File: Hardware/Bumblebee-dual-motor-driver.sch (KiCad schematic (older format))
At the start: 49 parts, among them J1 ICSP, J10 GND, J11 MOTOR1_A, J12 MOTOR1_B, J13 MOTOR2_A, J14 MOTOR2_B, J15 MAIN+, J16 MAIN-, J2 USB_B_Micro, J3 HEADER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

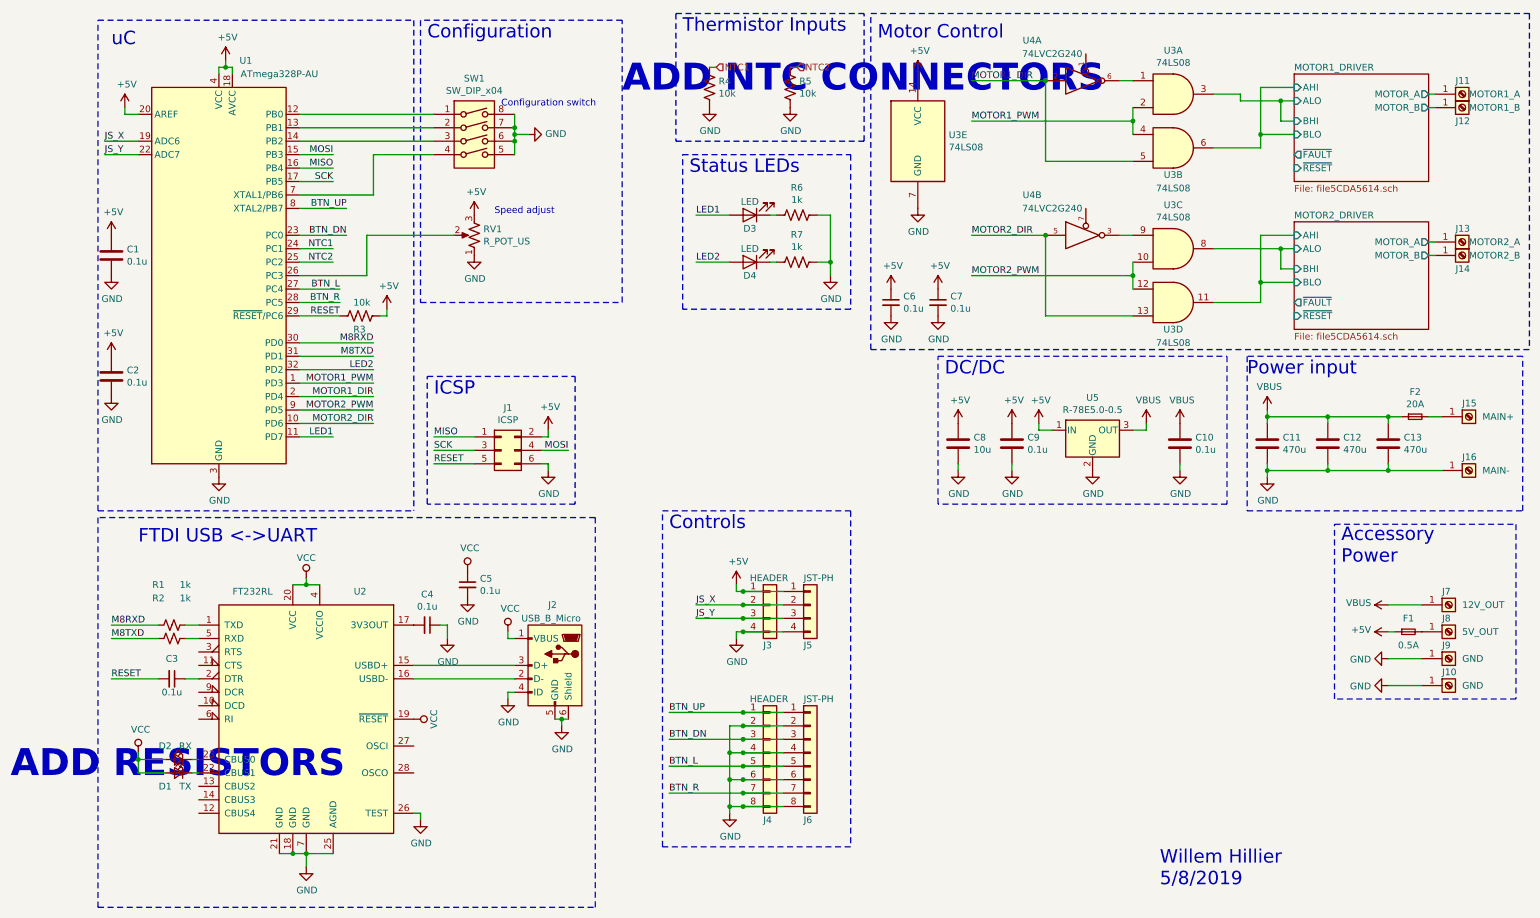
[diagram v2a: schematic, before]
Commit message: Fixed small issues and started laying out H-bridge
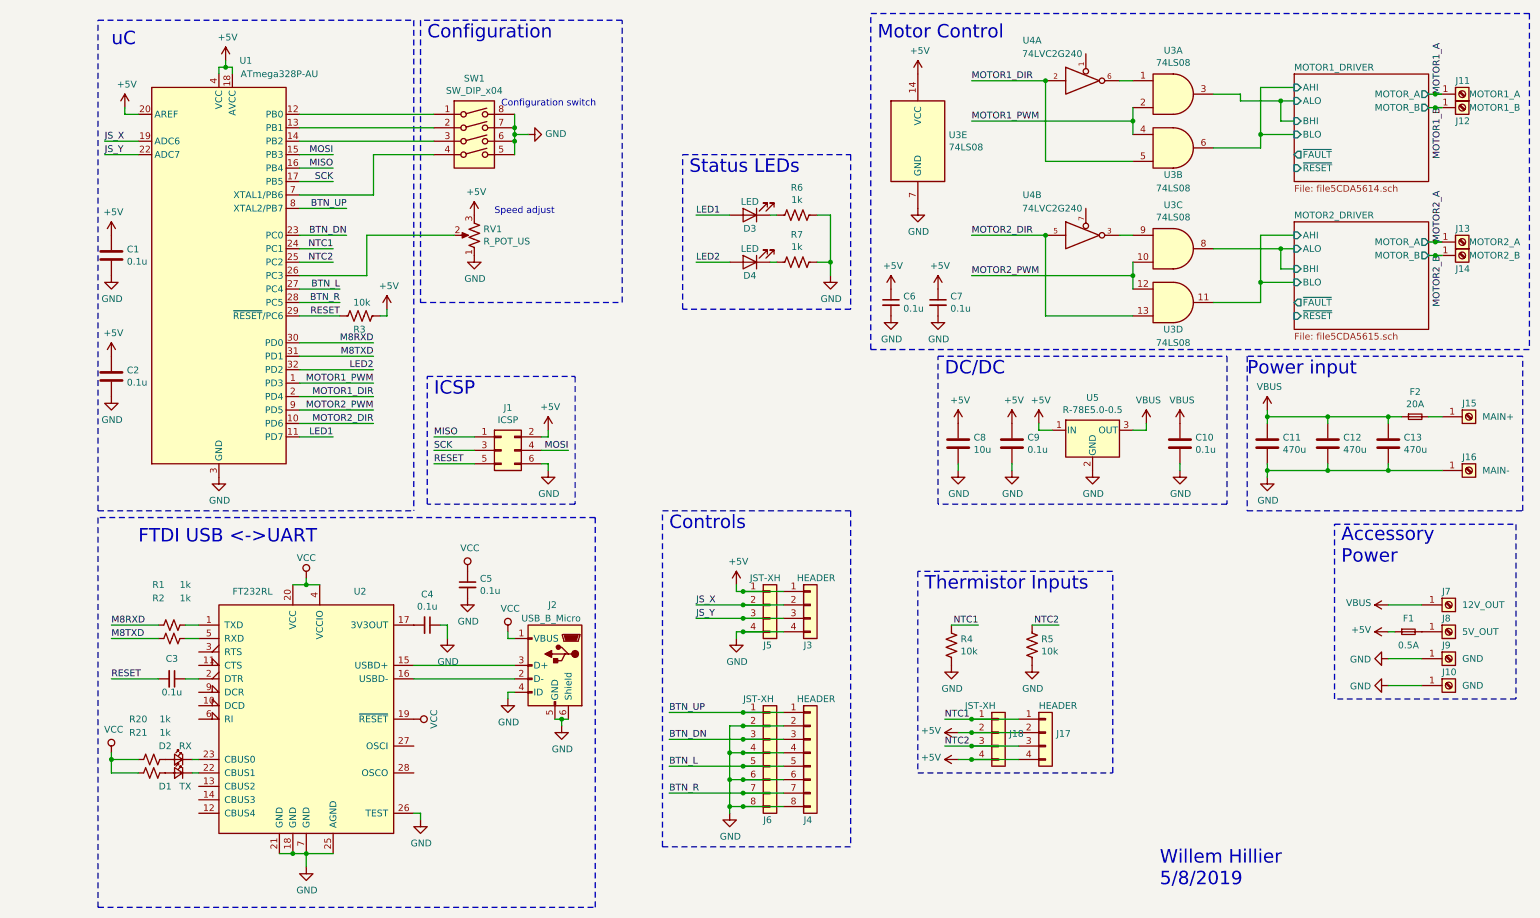
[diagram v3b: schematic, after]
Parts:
- added J17: HEADER, TerminalBlock_TE-Connectivity:TerminalBlock_TE_282834-4_1x04_P2.54mm_Horizontal, symbol Connector_Generic:Conn_01x04
- added J18: JST-XH, Connector_JST:JST_XH_B4B-XH-A_1x04_P2.50mm_Vertical, symbol Connector_Generic:Conn_01x04
- added R20, R21: 1k, Resistor_SMD:R_0603_1608Metric, symbol Device:R_Small_US
- J3: footprint Connector_PinSocket_2.54mm:PinSocket_1x04_P2.54mm_Vertical -> TerminalBlock_TE-Connectivity:TerminalBlock_TE_282834-4_1x04_P2.54mm_Horizontal
- J4: footprint Connector_PinSocket_2.54mm:PinSocket_1x08_P2.54mm_Vertical -> TerminalBlock_TE-Connectivity:TerminalBlock_TE_282834-8_1x08_P2.54mm_Horizontal
- J5, J6: value JST-PH -> JST-XH
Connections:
- net +5V: now also J17.2 (Pin_2), J17.4 (Pin_4), J18.2 (Pin_2), J18.4 (Pin_4)
- net NTC1: now also J17.1 (Pin_1), J18.1 (Pin_1)
- net NTC2: now also J17.3 (Pin_3), J18.3 (Pin_3)
- net VCC: now also R20.2, R21.2; no longer D1.2 (A), D2.2 (A)
- net MOTOR1_DRIVER/MOTOR_A renamed MOTOR1_A
- net MOTOR1_DRIVER/MOTOR_B renamed MOTOR1_B
- net MOTOR2_DRIVER/MOTOR_A renamed MOTOR2_A
- net MOTOR2_DRIVER/MOTOR_B renamed MOTOR2_B
- new net: D1.2 (A), R20.1
- new net: D2.2 (A), R21.1
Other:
- note removed: "ADD NTC CONNECTORS"
- note removed: "ADD RESISTORS"
- moved on the sheet: J3, J4, J5, J6, R4, R5
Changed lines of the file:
@@
 L Device:R_US R?
 U 1 1 5C53D9DB
-P 5100 1050
+P 6900 5200
 AR Path="/5C4E5628/5C53D9DB" Ref="R?"  Part="1"
 AR Path="/5C83278E/5C8304A7/5C53D9DB" Ref="R?"  Part="1"
 AR Path="/5C53D9DB" Ref="R4"  Part="1"
-F 0 "R4" H 5032 1004 50  0000 R CNN
-F 1 "10k" H 5032 1095 50  0000 R CNN
-F 2 "Resistor_SMD:R_0603_1608Metric" V 5140 1040 50  0001 C CNN
-F 3 "~" H 5100 1050 50  0001 C CNN
-	1    5100 1050
+F 0 "R4" H 6832 5154 50  0000 R CNN
+F 1 "10k" H 6832 5245 50  0000 R CNN
+F 2 "Resistor_SMD:R_0603_1608Metric" V 6940 5190 50  0001 C CNN
+F 3 "~" H 6900 5200 50  0001 C CNN
+	1    6900 5200
 	-1   0    0    1
 $EndComp
@@
 L power:GND #PWR?
 U 1 1 5C540E62
-P 5100 1200
+P 6900 5350
 AR Path="/5C4E5628/5C540E62" Ref="#PWR?"  Part="1"
 AR Path="/5C83278E/5C8304A7/5C540E62" Ref="#PWR?"  Part="1"
 AR Path="/5C540E62" Ref="#PWR025"  Part="1"
-F 0 "#PWR025" H 5100 950 50  0001 C CNN
-F 1 "GND" H 5105 1027 50  0000 C CNN
-F 2 "" H 5100 1200 50  0001 C CNN
-F 3 "" H 5100 1200 50  0001 C CNN
-	1    5100 1200
+F 0 "#PWR025" H 6900 5100 50  0001 C CNN
+F 1 "GND" H 6905 5177 50  0000 C CNN
+F 2 "" H 6900 5350 50  0001 C CNN
+F 3 "" H 6900 5350 50  0001 C CNN
+	1    6900 5350
 	1    0    0    -1
 $EndComp
@@
 L Device:R_US R?
 U 1 1 5C5485A4
-P 5700 1050
+P 7500 5200
 AR Path="/5C4E5628/5C5485A4" Ref="R?"  Part="1"
 AR Path="/5C83278E/5C8304A7/5C5485A4" Ref="R?"  Part="1"
 AR Path="/5C5485A4" Ref="R5"  Part="1"
-F 0 "R5" H 5632 1004 50  0000 R CNN
-F 1 "10k" H 5632 1095 50  0000 R CNN
-F 2 "Resistor_SMD:R_0603_1608Metric" V 5740 1040 50  0001 C CNN
-F 3 "~" H 5700 1050 50  0001 C CNN
-	1    5700 1050
+F 0 "R5" H 7432 5154 50  0000 R CNN
+F 1 "10k" H 7432 5245 50  0000 R CNN
+F 2 "Resistor_SMD:R_0603_1608Metric" V 7540 5190 50  0001 C CNN
+F 3 "~" H 7500 5200 50  0001 C CNN
+	1    7500 5200
 	-1   0    0    1
 $EndComp
@@
 L power:GND #PWR?
 U 1 1 5C5485BA
-P 5700 1200
+P 7500 5350
 AR Path="/5C4E5628/5C5485BA" Ref="#PWR?"  Part="1"
 AR Path="/5C83278E/5C8304A7/5C5485BA" Ref="#PWR?"  Part="1"
 AR Path="/5C5485BA" Ref="#PWR029"  Part="1"
-F 0 "#PWR029" H 5700 950 50  0001 C CNN
-F 1 "GND" H 5705 1027 50  0000 C CNN
-F 2 "" H 5700 1200 50  0001 C CNN
-F 3 "" H 5700 1200 50  0001 C CNN
-	1    5700 1200
+F 0 "#PWR029" H 7500 5100 50  0001 C CNN
+F 1 "GND" H 7505 5177 50  0000 C CNN
+F 2 "" H 7500 5350 50  0001 C CNN
+F 3 "" H 7500 5350 50  0001 C CNN
+	1    7500 5350
 	1    0    0    -1
 $EndComp
@@
 Wire Notes Line
 	550  4200 2900 4200
-Text Notes 4900 650  0    100  ~ 0
+Text Notes 6700 4800 0    100  ~ 0
 Thermistor Inputs
-Text HLabel 5150 900  2    50   Input ~ 0
-NTC1
-Wire Wire Line
-	5150 900  5100 900
-Text HLabel 5750 900  2    50   Input ~ 0
-NTC2
-Wire Wire Line
-	5750 900  5700 900
-Wire Notes Line
-	4850 500  6250 500
-Wire Notes Line
-	4850 500  4850 1450
-Wire Notes Line
-	4850 1450 6250 1450
-Wire Notes Line
-	6250 1450 6250 500
 Text Notes 8450 7000 0    100  ~ 0
 Willem Hillier\n5/8/2019
@@
 L Connector_Generic:Conn_01x04 J5
 U 1 1 5CEF2069
-P 5850 4900
-F 0 "J5" H 5800 4600 50  0000 L CNN
-F 1 "JST-PH" H 5800 5100 50  0000 L CNN
-F 2 "Connector_JST:JST_XH_B4B-XH-A_1x04_P2.50mm_Vertical" H 5850 4900 50  0001 C CNN
-F 3 "~" H 5850 4900 50  0001 C CNN
-	1    5850 4900
+P 5550 4900
+F 0 "J5" H 5500 4600 50  0000 L CNN
+F 1 "JST-XH" H 5400 5100 50  0000 L CNN
+F 2 "Connector_JST:JST_XH_B4B-XH-A_1x04_P2.50mm_Vertical" H 5550 4900 50  0001 C CNN
+F 3 "~" H 5550 4900 50  0001 C CNN
+	1    5550 4900
 	1    0    0    -1
 $EndComp
@@
 L Connector_Generic:Conn_01x04 J3
 U 1 1 5CEFCADE
-P 5550 4900
-F 0 "J3" H 5500 4600 50  0000 L CNN
-F 1 "HEADER" H 5400 5100 50  0000 L CNN
-F 2 "Connector_PinSocket_2.54mm:PinSocket_1x04_P2.54mm_Vertical" H 5550 4900 50  0001 C CNN
-F 3 "~" H 5550 4900 50  0001 C CNN
-	1    5550 4900
+P 5850 4900
+F 0 "J3" H 5800 4600 50  0000 L CNN
+F 1 "HEADER" H 5750 5100 50  0000 L CNN
+F 2 "TerminalBlock_TE-Connectivity:TerminalBlock_TE_282834-4_1x04_P2.54mm_Horizontal" H 5850 4900 50  0001 C CNN
+F 3 "~" H 5850 4900 50  0001 C CNN
+	1    5850 4900
 	1    0    0    -1
 $EndComp
@@
 L power:VCC #PWR06
 U 1 1 5CFB0C44
-P 850 6000
-F 0 "#PWR06" H 850 5850 50  0001 C CNN
-F 1 "VCC" H 867 6173 50  0000 C CNN
-F 2 "" H 850 6000 50  0001 C CNN
-F 3 "" H 850 6000 50  0001 C CNN
-	1    850  6000
-	1    0    0    -1
-$EndComp
-Wire Wire Line
-	850  6000 850  6050
-Wire Wire Line
-	850  6050 1050 6050
-Wire Wire Line
-	1050 6150 850  6150
-Wire Wire Line
-	850  6150 850  6050
-Connection ~ 850  6050
+P 650 6000
+F 0 "#PWR06" H 650 5850 50  0001 C CNN
+F 1 "VCC" H 667 6173 50  0000 C CNN
+F 2 "" H 650 6000 50  0001 C CNN
+F 3 "" H 650 6000 50  0001 C CNN
+	1    650  6000
+	1    0    0    -1
+$EndComp
+Wire Wire Line
+	650  6000 650  6050
+Wire Wire Line
+	650  6050 850  6050
+Wire Wire Line
+	850  6150 650  6150
+Wire Wire Line
+	650  6150 650  6050
+Connection ~ 650  6050
 Text Label 650  5050 0    50   ~ 0
 M8RXD
@@
 L Connector_Generic:Conn_01x08 J4
 U 1 1 5D13B745
-P 5550 6000
-F 0 "J4" H 5500 5500 50  0000 L CNN
-F 1 "HEADER" H 5400 6400 50  0000 L CNN
-F 2 "Connector_PinSocket_2.54mm:PinSocket_1x08_P2.54mm_Vertical" H 5550 6000 50  0001 C CNN
-F 3 "~" H 5550 6000 50  0001 C CNN
-	1    5550 6000
-	1    0    0    -1
-$EndComp
-$Comp
-L Connector_Generic:Conn_01x08 J6
-U 1 1 5D13C2EF
 P 5850 6000
-F 0 "J6" H 5800 5500 50  0000 L CNN
-F 1 "JST-PH" H 5800 6400 50  0000 L CNN
-F 2 "Connector_JST:JST_XH_B8B-XH-A_1x08_P2.50mm_Vertical" H 5850 6000 50  0001 C CNN
+F 0 "J4" H 5800 5500 50  0000 L CNN
+F 1 "HEADER" H 5750 6400 50  0000 L CNN
+F 2 "TerminalBlock_TE-Connectivity:TerminalBlock_TE_282834-8_1x08_P2.54mm_Horizontal" H 5850 6000 50  0001 C CNN
 F 3 "~" H 5850 6000 50  0001 C CNN
 	1    5850 6000
@@
 Wire Wire Line
 	5650 6300 5350 6300
-Wire Wire Line
-	5350 6400 5650 6400
-Connection ~ 5350 6400
 Connection ~ 5350 6200
 Connection ~ 5350 6000
@@
 	5250 5800 5250 6000
 Wire Wire Line
-	5250 6400 5350 6400
-Wire Wire Line
 	5250 5800 5350 5800
 $Comp
@@
 U 5D4DF0EE
 F0 "MOTOR2_DRIVER" 50
-F1 "file5CDA5614.sch" 50
+F1 "file5CDA5615.sch" 50
 F2 "AHI" I L 9450 2150 50
 F3 "ALO" I L 9450 2250 50
@@
 Text Notes 3000 700  0    100  ~ 0
 Configuration
-Text Notes -100 6200 0    200  ~ 40
-ADD RESISTORS
-Text Notes 4450 1100 0    200  ~ 40
-ADD NTC CONNECTORS
+$Comp
+L Device:R_Small_US R20
+U 1 1 5CD595B4
+P 950 6050
+F 0 "R20" V 650 5950 50  0000 C CNN
+F 1 "1k" V 650 6150 50  0000 C CNN
+F 2 "Resistor_SMD:R_0603_1608Metric" H 950 6050 50  0001 C CNN
+F 3 "~" H 950 6050 50  0001 C CNN
+	1    950  6050
+	0    1    1    0
+$EndComp
+$Comp
+L Device:R_Small_US R21
+U 1 1 5CD595BA
+P 950 6150
+F 0 "R21" V 650 6050 50  0000 C CNN
+F 1 "1k" V 650 6250 50  0000 C CNN
+F 2 "Resistor_SMD:R_0603_1608Metric" H 950 6150 50  0001 C CNN
+F 3 "~" H 950 6150 50  0001 C CNN
+	1    950  6150
+	0    1    1    0
+$EndComp
+$Comp
+L Connector_Generic:Conn_01x04 J17
+U 1 1 5CD7FE91
+P 7600 5850
+F 0 "J17" H 7680 5842 50  0000 L CNN
+F 1 "HEADER" H 7550 6050 50  0000 L CNN
+F 2 "TerminalBlock_TE-Connectivity:TerminalBlock_TE_282834-4_1x04_P2.54mm_Horizontal" H 7600 5850 50  0001 C CNN
+F 3 "~" H 7600 5850 50  0001 C CNN
+	1    7600 5850
+	1    0    0    -1
+$EndComp
+Text Label 7100 5050 2    50   ~ 0
+NTC1
+Text Label 7700 5050 2    50   ~ 0
+NTC2
+Wire Wire Line
+	6900 5050 7100 5050
+Wire Wire Line
+	7500 5050 7700 5050
+Text Label 6850 5750 0    50   ~ 0
+NTC1
+Text Label 6850 5950 0    50   ~ 0
+NTC2
+$Comp
+L power:+5V #PWR0101
+U 1 1 5CDE3A51
+P 6950 5850
+F 0 "#PWR0101" H 6950 5700 50  0001 C CNN
+F 1 "+5V" V 6965 5978 50  0000 L CNN
+F 2 "" H 6950 5850 50  0001 C CNN
+F 3 "" H 6950 5850 50  0001 C CNN
+	1    6950 5850
+	0    -1   -1   0
+$EndComp
+$Comp
+L power:+5V #PWR0102
+U 1 1 5CDF0FB8
+P 6950 6050
+F 0 "#PWR0102" H 6950 5900 50  0001 C CNN
+F 1 "+5V" V 6965 6178 50  0000 L CNN
+F 2 "" H 6950 6050 50  0001 C CNN
+F 3 "" H 6950 6050 50  0001 C CNN
+	1    6950 6050
+	0    -1   -1   0
+$EndComp
+Wire Notes Line
+	6650 4650 6650 6150
+Wire Notes Line
+	6650 6150 8100 6150
+Wire Notes Line
+	8100 6150 8100 4650
+Wire Notes Line
+	8100 4650 6650 4650
+Connection ~ 7050 6050
+Connection ~ 7050 5850
+Connection ~ 7050 5950
+Connection ~ 7050 5750
+Wire Wire Line
+	6950 6050 7050 6050
+Wire Wire Line
+	7050 6050 7400 6050
+Wire Wire Line
+	6850 5950 7050 5950
+Wire Wire Line
+	7050 5950 7400 5950
+Wire Wire Line
+	6950 5850 7050 5850
+Wire Wire Line
+	7050 5850 7400 5850
+Wire Wire Line
+	6850 5750 7050 5750
+Wire Wire Line
+	7400 5750 7050 5750
+$Comp
+L Connector_Generic:Conn_01x04 J18
+U 1 1 5CD80270
+P 7250 5850
+F 0 "J18" H 7330 5842 50  0000 L CNN
+F 1 "JST-XH" H 7000 6050 50  0000 L CNN
+F 2 "Connector_JST:JST_XH_B4B-XH-A_1x04_P2.50mm_Vertical" H 7250 5850 50  0001 C CNN
+F 3 "~" H 7250 5850 50  0001 C CNN
+	1    7250 5850
+	1    0    0    -1
+$EndComp
+Connection ~ 5350 6400
+Wire Wire Line
+	5250 6400 5350 6400
+Wire Wire Line
+	5350 6400 5650 6400
+$Comp
+L Connector_Generic:Conn_01x08 J6
+U 1 1 5D13C2EF
+P 5550 6000
+F 0 "J6" H 5500 5500 50  0000 L CNN
+F 1 "JST-XH" H 5350 6400 50  0000 L CNN
+F 2 "Connector_JST:JST_XH_B8B-XH-A_1x08_P2.50mm_Vertical" H 5550 6000 50  0001 C CNN
+F 3 "~" H 5550 6000 50  0001 C CNN
+	1    5550 6000
+	1    0    0    -1
+$EndComp
+Text Label 10550 1100 1    50   ~ 0
+MOTOR1_A
+Text Label 10550 1200 3    50   ~ 0
+MOTOR1_B
+Wire Wire Line
+	10550 1100 10500 1100
+Connection ~ 10500 1100
+Wire Wire Line
+	10500 1200 10550 1200
+Connection ~ 10500 1200
+Text Label 10550 2300 3    50   ~ 0
+MOTOR2_B
+Text Label 10550 2200 1    50   ~ 0
+MOTOR2_A
+Wire Wire Line
+	10550 2200 10500 2200
+Connection ~ 10500 2200
+Wire Wire Line
+	10500 2300 10550 2300
+Connection ~ 10500 2300
 $EndSCHEMATC

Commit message: Further progress laying out Bumblebee
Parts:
- R1, R2, R20, R21: symbol Device:R_Small_US -> Bumblebee-dual-motor-driver-rescue:R_Small_US-Device
- U2: symbol Interface_USB:FT232RL -> Bumblebee-dual-motor-driver-rescue:FT232RL-Interface_USB
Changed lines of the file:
@@
 EESchema Schematic File Version 4
 LIBS:Bumblebee-dual-motor-driver-cache
-EELAYER 29 0
+EELAYER 26 0
 EELAYER END
 $Descr A4 11693 8268
@@
 JS_Y
 $Comp
-L Interface_USB:FT232RL U2
+L Bumblebee-dual-motor-driver-rescue:FT232RL-Interface_USB U2
 U 1 1 5CF29FD7
 P 2100 5750
@@
 M8RXD
 $Comp
-L Device:R_Small_US R1
+L Bumblebee-dual-motor-driver-rescue:R_Small_US-Device R1
 U 1 1 5CFBCE5C
 P 1100 5050
@@
 $EndComp
 $Comp
-L Device:R_Small_US R2
+L Bumblebee-dual-motor-driver-rescue:R_Small_US-Device R2
 U 1 1 5CFBD8D4
 P 1100 5150
@@
 Configuration
 $Comp
-L Device:R_Small_US R20
+L Bumblebee-dual-motor-driver-rescue:R_Small_US-Device R20
 U 1 1 5CD595B4
 P 950 6050
@@
 $EndComp
 $Comp
-L Device:R_Small_US R21
+L Bumblebee-dual-motor-driver-rescue:R_Small_US-Device R21
 U 1 1 5CD595BA
 P 950 6150

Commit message: Finished routing board. Need to still do documentation.
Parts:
- J1: footprint Connector_PinSocket_2.54mm:PinSocket_2x03_P2.54mm_Vertical -> Connector_PinHeader_2.54mm:PinHeader_2x03_P2.54mm_Vertical
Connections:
- net +5V: now also R20.2, R21.2, U2.19 (~RESET~), U4.8 (VCC), U4.8 (VCC)
- net JS_X: now also U1.22 (ADC7); no longer U1.19 (ADC6)
- net JS_Y: now also U1.19 (ADC6); no longer U1.22 (ADC7)
- net NTC1: now also U1.25 (PC2); no longer U1.24 (PC1)
- net NTC2: now also U1.24 (PC1); no longer U1.25 (PC2)
- net at U1.12 (PB0): now also SW1.3; no longer SW1.1
- net at U1.14 (PB2): now also SW1.1; no longer SW1.3
- removed net VCC: C5.1, J2.1 (VBUS), R20.2, R21.2, U2.19 (~RESET~), U2.20 (VCC), U2.4 (VCCIO), U4.8 (VCC), U4.8 (VCC)
- new net USB_PWR: C5.1, J2.1 (VBUS), U2.20 (VCC), U2.4 (VCCIO)
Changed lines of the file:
@@
 F 0 "J1" H 3600 4067 50  0000 C CNN
 F 1 "ICSP" H 3600 3976 50  0000 C CNN
-F 2 "Connector_PinSocket_2.54mm:PinSocket_2x03_P2.54mm_Vertical" H 3550 3750 50  0001 C CNN
+F 2 "Connector_PinHeader_2.54mm:PinHeader_2x03_P2.54mm_Vertical" H 3550 3750 50  0001 C CNN
 F 3 "~" H 3550 3750 50  0001 C CNN
 	1    3550 3750
@@
 Wire Wire Line
 	2050 3150 2600 3150
+Text Label 2300 2350 2    50   ~ 0
+NTC1
 Text Label 2300 2250 2    50   ~ 0
-NTC1
-Text Label 2300 2350 2    50   ~ 0
 NTC2
 Wire Wire Line
@@
 	1    0    0    -1
 $EndComp
-Wire Wire Line
-	2050 1350 3050 1350
-Wire Wire Line
-	2050 1450 3050 1450
 Wire Wire Line
 	3050 1550 2600 1550
@@
 Text Notes 3550 1200 0    50   ~ 0
 Configuration switch
-Wire Wire Line
-	2050 1250 3050 1250
 $Comp
 L Device:R_POT_US RV1
@@
 Wire Wire Line
 	850  1550 600  1550
+Text Label 600  1550 0    50   ~ 0
+JS_X
 Text Label 600  1450 0    50   ~ 0
-JS_X
-Text Label 600  1550 0    50   ~ 0
 JS_Y
 $Comp
@@
 Wire Wire Line
 	2100 6850 2100 6750
-$Comp
-L power:VCC #PWR09
-U 1 1 5CF6F5A6
-P 2100 4700
-F 0 "#PWR09" H 2100 4550 50  0001 C CNN
-F 1 "VCC" H 2100 4850 50  0000 C CNN
-F 2 "" H 2100 4700 50  0001 C CNN
-F 3 "" H 2100 4700 50  0001 C CNN
-	1    2100 4700
-	1    0    0    -1
-$EndComp
 Wire Wire Line
 	2100 4700 2100 4750
@@
 F 3 "" H 3300 4850 50  0001 C CNN
 	1    3300 4850
-	1    0    0    -1
-$EndComp
-$Comp
-L power:VCC #PWR015
-U 1 1 5CF7DAA5
-P 3300 4650
-F 0 "#PWR015" H 3300 4500 50  0001 C CNN
-F 1 "VCC" H 3317 4823 50  0000 C CNN
-F 2 "" H 3300 4650 50  0001 C CNN
-F 3 "" H 3300 4650 50  0001 C CNN
-	1    3300 4650
-	1    0    0    -1
-$EndComp
-$Comp
-L power:VCC #PWR019
-U 1 1 5CF7E72B
-P 3600 5100
-F 0 "#PWR019" H 3600 4950 50  0001 C CNN
-F 1 "VCC" H 3617 5273 50  0000 C CNN
-F 2 "" H 3600 5100 50  0001 C CNN
-F 3 "" H 3600 5100 50  0001 C CNN
-	1    3600 5100
 	1    0    0    -1
 $EndComp
@@
 	10500 2300 10550 2300
 Connection ~ 10500 2300
+$Comp
+L power:+5V #PWR0117
+U 1 1 5CD5EFC5
+P 7950 750
+F 0 "#PWR0117" H 7950 600 50  0001 C CNN
+F 1 "+5V" H 7965 923 50  0000 C CNN
+F 2 "" H 7950 750 50  0001 C CNN
+F 3 "" H 7950 750 50  0001 C CNN
+	1    7950 750
+	1    0    0    -1
+$EndComp
+Wire Wire Line
+	7950 750  7950 950
+Wire Wire Line
+	3050 1250 2300 1250
+Wire Wire Line
+	2300 1250 2300 1450
+Wire Wire Line
+	2300 1450 2050 1450
+Wire Wire Line
+	2050 1350 3050 1350
+Wire Wire Line
+	3050 1450 2600 1450
+Wire Wire Line
+	2600 1450 2600 1300
+Wire Wire Line
+	2600 1300 2150 1300
+Wire Wire Line
+	2150 1300 2150 1250
+Wire Wire Line
+	2150 1250 2050 1250
+Text Label 3600 5100 1    50   ~ 0
+USB_PWR
+Text Label 3300 4650 1    50   ~ 0
+USB_PWR
+Text Label 2100 4700 2    50   ~ 0
+USB_PWR
 $EndSCHEMATC
